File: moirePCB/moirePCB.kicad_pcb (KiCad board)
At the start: 4 copper layers, 32 x 228.8 mm, 57 parts, among them J1 USB_C_Receptacle, U1 ESP32-PICO-D4, U10 TLV73333PDBV, U2 BQ25504, U3 TLV73333PDBV, U4 RFM95W-915S2, U5 CH340E, U6 TLC555xD, U7 HDC1080, U8 AP2281-1WG-7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

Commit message: PCB 3
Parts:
- removed MNT_1, MNT_2: MountingHole_2.2mm_M2_Pad_Via, MountingHole:MountingHole_2.2mm_M2_Pad_Via
- added MNTL: MountingHole_2.2mm_M2_Pad_Via, MountingHole:MountingHole_2.2mm_M2_Pad_Via, F.Cu at (55.1, 122.0)
- added MNTU: MountingHole_2.2mm_M2_Pad_Via, MountingHole:MountingHole_2.2mm_M2_Pad_Via, F.Cu at (60.2, 39.0)
- moved R6 72.7 mm to (65.4, 31.9), turned to 180 degrees
- moved EN1 58.5 mm to (47.0, 57.6)
- moved BT1 56.2 mm to (39.5, 112.2), turned to -90 degrees
- moved U8 54.2 mm to (65.4, 47.6)
- moved R7 52.6 mm to (65.8, 51.4)
- moved R4 39.0 mm to (71.1, 68.6), turned to 180 degrees
- moved U7 35.4 mm to (70.1, 49.0)
- moved R_OK_1 26.6 mm to (67.8, 113.9)
- moved R_OV_1 20.2 mm to (61.4, 109.7)
- moved C_STOR1 19.5 mm to (61.0, 113.5)
- moved C5 19.3 mm to (60.3, 43.7)
- moved C7 19.3 mm to (60.4, 50.2)
- moved C1 19.3 mm to (60.3, 46.9)
- moved R_OC+10 19.1 mm to (49.0, 116.6), turned to 0 degrees
- moved FREQOUT_JP1 17.8 mm to (63.0, 126.9)
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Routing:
- net PROBE: track 17.4 -> 134.3 mm
- net FREQOUT: track 196.5 -> 94.9 mm
- net Net-(J1-CC2): track 76.4 -> 7.83 mm, vias 2 -> 0
- net Net-(J1-CC1): track 75.9 -> 15.6 mm, vias 2 -> 0
- net /EN: track 81.6 -> 28.9 mm, vias 3 -> 2
- net BATT_MEASURE: track 77.6 -> 25.1 mm, vias 3 -> 0
- net Net-(BT1-+): track 64.2 -> 107.0 mm
- net Net-(BATTMEASURE_JP1-B): track 61.5 -> 25.3 mm, vias 2 -> 0
- net Net-(TEMP_SDA_JP1-A): track 9.60 -> 34.7 mm
- net Net-(U2-VBAT_OV): track 42.5 -> 19.6 mm
- net Net-(SC1-+): track 124.7 -> 103.2 mm
- net Net-(R_OC+10-Pad1): track 23.7 -> 2.45 mm, vias 2 -> 0
- net VCC: track 162.2 -> 141.9 mm
- net Net-(U2-VOC_SAMP): track 29.5 -> 10.1 mm, vias 2 -> 0
- net A_VCC: track 146.6 -> 164.7 mm
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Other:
- board size 32 x 228.8 mm -> 38 x 215.8 mm
- board text removed: "solar//usb"

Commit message: pcb3 prod
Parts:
- BT1: footprint Connector_JST:JST_EH_S2B-EH_1x02_P2.50mm_Horizontal -> Connector_JST:JST_PH_S2B-PH-K_1x02_P2.00mm_Horizontal
- moved BT1 1.89 mm to (39.5, 114.0), turned to 90 degrees
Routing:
- net Net-(BT1-+): track 107.0 -> 105.9 mm

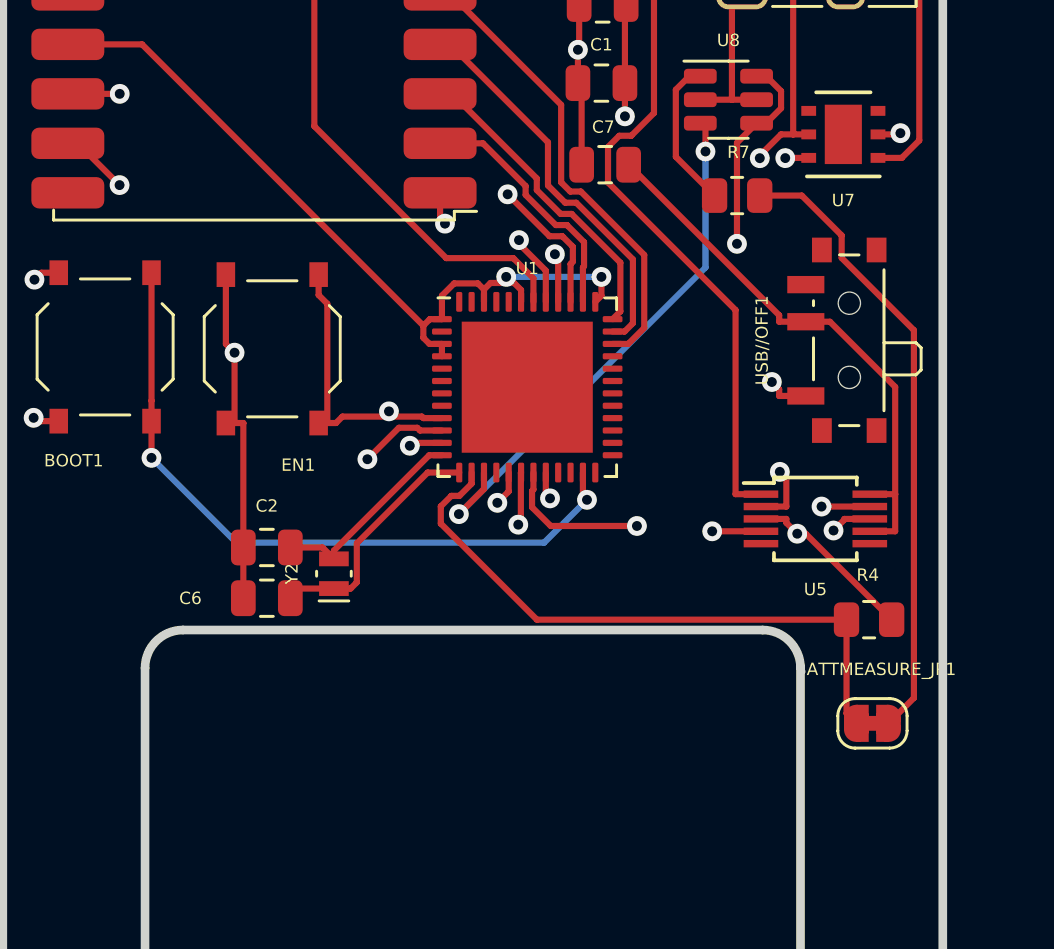
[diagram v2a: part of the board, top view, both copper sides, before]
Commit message: pcb4: add grounding to esp32
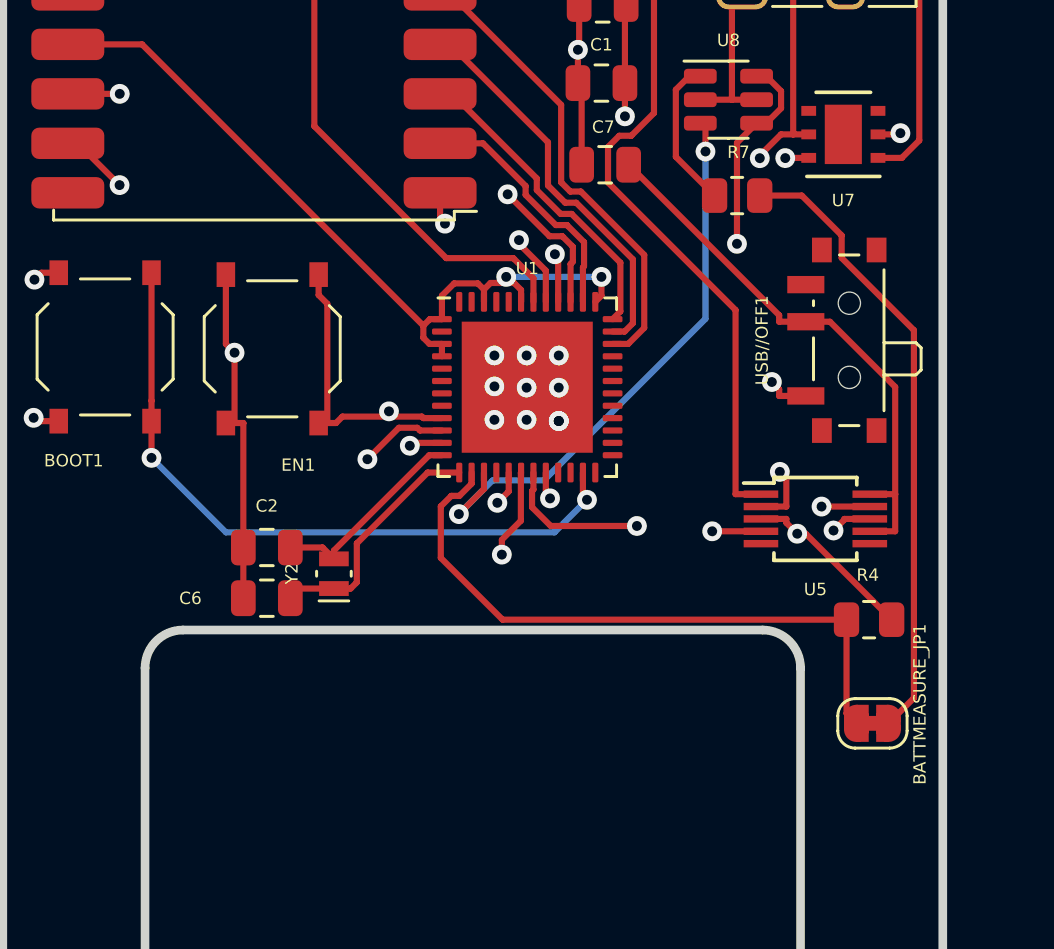
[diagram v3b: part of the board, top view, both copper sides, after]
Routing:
- net Net-(SC1-+): track 103.2 -> 105.1 mm
- net /GPIO_12: track 26.8 -> 28.6 mm
- net Net-(BT1-+): track 105.9 -> 107.4 mm
- net /GPIO_14: track 26.7 -> 27.9 mm
- net ACCESSORY_SW: track 81.0 -> 82.3 mm
- net BATT_MEASURE: track 25.1 -> 26.0 mm
- net GND: vias 17 -> 27

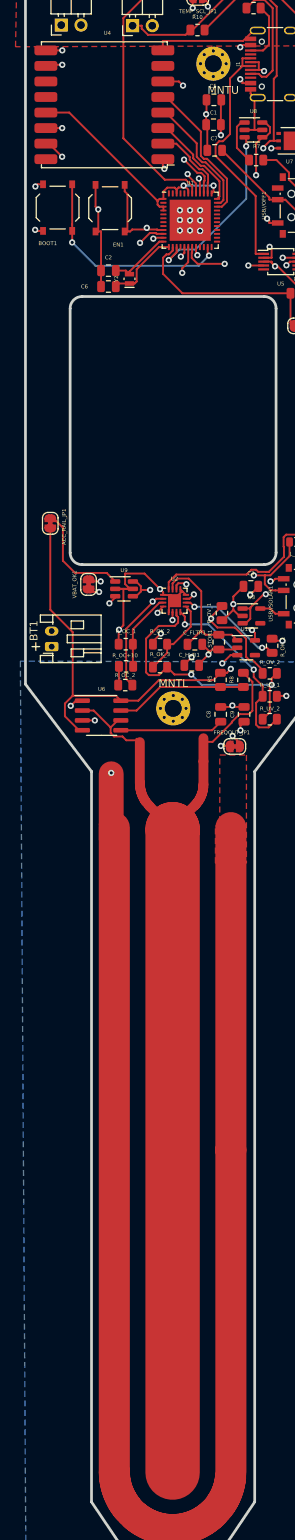
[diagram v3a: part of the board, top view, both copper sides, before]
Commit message: PCB 4: Silkscreen, part #s
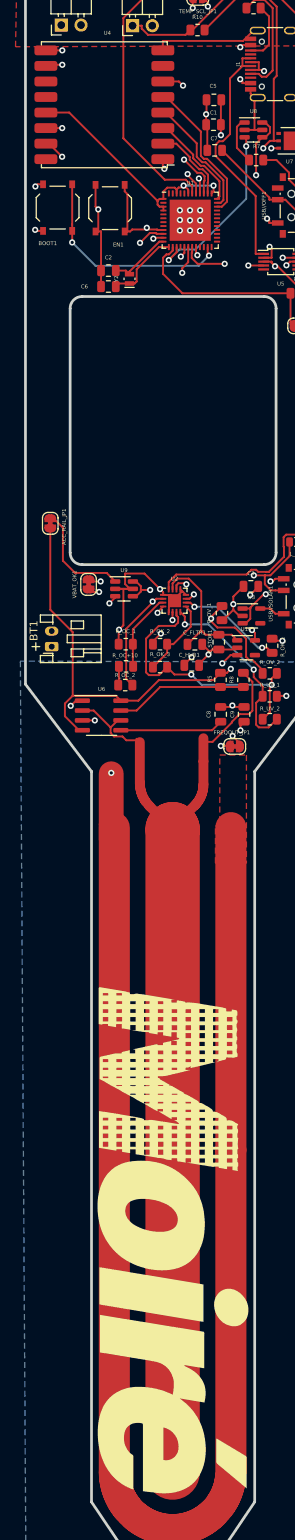
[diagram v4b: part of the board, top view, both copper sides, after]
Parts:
- removed MNTL, MNTU: MountingHole_2.2mm_M2_Pad_Via, MountingHole:MountingHole_2.2mm_M2_Pad_Via

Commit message: pcb-100
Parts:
- added REF**: MountingHole_3.2mm_M3_DIN965_Pad, MountingHole:MountingHole_3.2mm_M3_DIN965_Pad, F.Cu at (59.3, 39.4)
- added REF**: MountingHole_3.2mm_M3_DIN965_Pad, MountingHole:MountingHole_3.2mm_M3_DIN965_Pad, F.Cu at (55.1, 122.4)
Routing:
- net Net-(U6-CV): track 13.3 -> 16.2 mm
- net FREQOUT: track 94.9 -> 97.2 mm
- net Net-(FREQOUT_JP1-B): track 21.9 -> 23.3 mm
- net /GPIO_22: track 27.1 -> 27.8 mm
